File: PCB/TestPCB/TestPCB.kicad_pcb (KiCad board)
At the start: 2 copper layers, 19 parts, among them M2 Screw MountingHole_2.2mm_M2

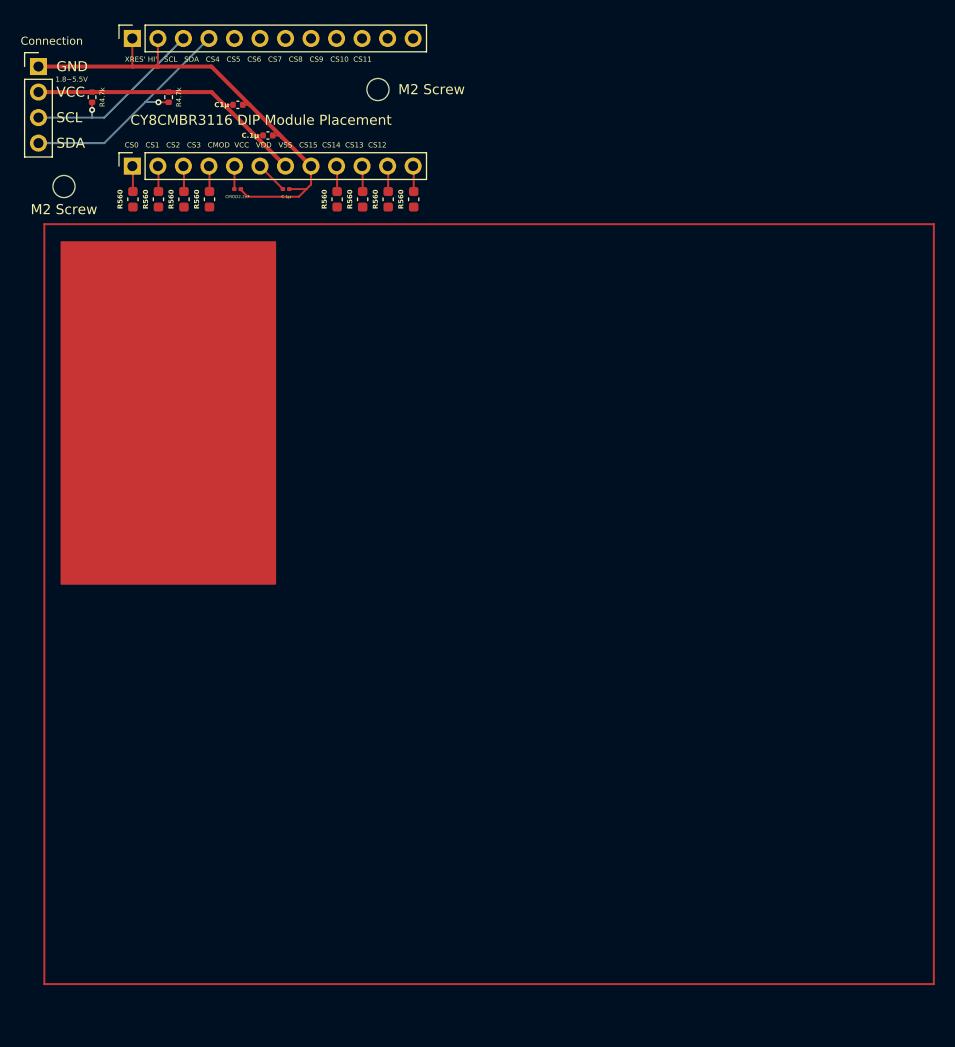
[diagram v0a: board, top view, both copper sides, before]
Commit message: Organize code & improve latency
+ IMPROVED LATENCY from 70~75ms to 40ms
- Removed old unused code
+ A few comments
+ 3rd party library tweak method on README.md
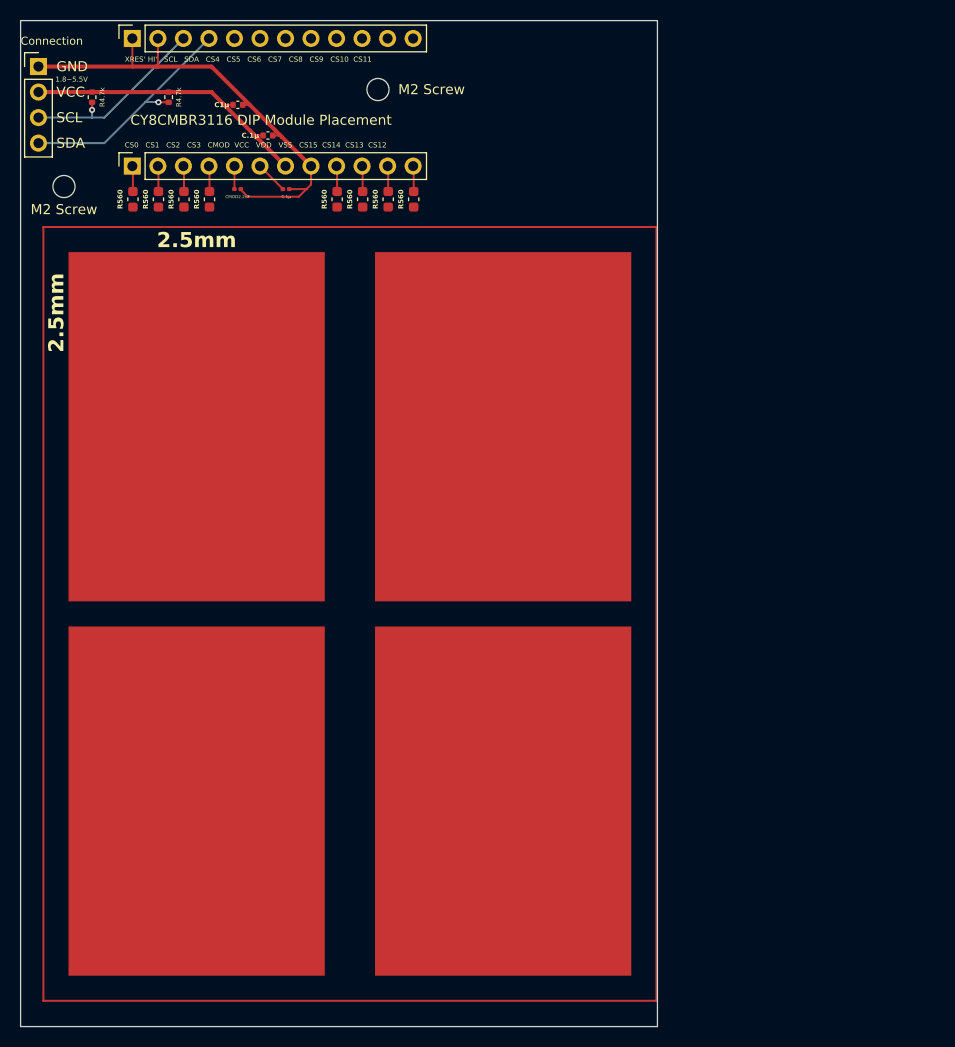
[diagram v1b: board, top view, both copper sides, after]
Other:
- board outline added: 63.4 x 100.1 mm
- board text added: "2.5mm"
